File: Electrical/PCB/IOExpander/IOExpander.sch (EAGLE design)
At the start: 38 parts, among them U1 MCP23017T-E/SS

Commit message: PCB Batch #1
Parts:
- added A0A1, A2A3, A4A5, A6A7, IA16, IA17, IA18, IA19, IA20, IA21, IA22, IA23, IB16, IB17, IB18, IB19, IB20, IB21, IB22, IB23: JST_1.25_3P, Scott-Connectors:JST_1.25_3P
- added F1, F3: (no value), Scott-Electrical:FUSE-0603
- added H1, H2, H3, H4: HOLE-M3, Scott-Mechanical:HOLE-M3
- added LA16, LA17, LA18, LA19, LA20, LA21, LA22, LA23, LB16, LB17, LB18, LB19, LB20, LB21, LB22, LB23: JST_1.25_2P, Scott-Connectors:JST_1.25_2P
- added MCU2: JST_1.25_6P, Scott-Connectors:JST_1.25_6P
- added R1, R17, R19, R21, R23, R24, R3, R5, R7, R8: DNP, Scott-Electrical:RESISTOR0603
- added R18, R2, R20, R22, R4, R6: 10K, Scott-Electrical:RESISTOR0603
- added RA5, RA6: (no value), Scott-Electrical:RESISTOR_ARRAY_1206_SEPARATE
- added RB5, RB6: (no value), Scott-Electrical:RESISTOR_ARRAY_1206_SEPARATE_REVERSE
- added U3: MCP23017T-E/SS, Scott-ICs:MCP23017T-E/SS
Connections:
- new net ADDR0: R1.1, R2.2, U1.A0
- new net ADDR0_2: R17.1, R18.2, U3.A0
- new net ADDR1: R3.1, R4.2, U1.A1
- new net ADDR1_2: R19.1, R20.2, U3.A1
- new net ADDR2: R5.1, R6.2, U1.A2
- new net ADDR2_2: R21.1, R22.2, U3.A2
- new net C0: IA23.1, LA23.2, RA5@4.2
- new net C1: IA16.1, LA16.2, RA5@3.2
- new net C2: IA17.1, LA17.2, RA5@2.2
- new net C3: IA18.1, LA18.2, RA5@1.2
- new net C4: IA19.1, LA19.2, RA6@4.2
- new net C5: IA20.1, LA20.2, RA6@3.2
- new net C6: IA21.1, LA21.2, RA6@2.2
- new net C7: IA22.1, LA22.2, RA6@1.2
- new net D0: IB23.1, LB23.2, RB5@4.1
- new net D1: IB16.1, LB16.2, RB5@3.1
- new net D2: IB17.1, LB17.2, RB5@2.1
- new net D3: IB18.1, LB18.2, RB5@1.1
- new net D4: IB19.1, LB19.2, RB6@4.1
- new net D5: IB20.1, LB20.2, RB6@3.1
- new net D6: IB21.1, LB21.2, RB6@2.1
- new net D7: IB22.1, LB22.2, RB6@1.1
- new net INTC: MCU2.2, U3.INTA
- new net INTD: MCU2.1, U3.INTB
- new net N$35: RB5@1.2, U3.GPB3
- new net N$36: RB5@2.2, U3.GPB2
- new net N$37: RB5@3.2, U3.GPB1
- new net N$38: RB5@4.2, U3.GPB0
- new net N$39: RB6@1.2, U3.GPB7
- new net N$40: RB6@2.2, U3.GPB6
- new net N$41: RB6@3.2, U3.GPB5
- new net N$42: RB6@4.2, U3.GPB4
- new net N$43: RA5@1.1, U3.GPA3
- new net N$46: RA5@4.1, U3.GPA0
- new net N$47: RA6@1.1, U3.GPA7
- new net N$48: RA6@2.1, U3.GPA6
- new net N$49: RA6@3.1, U3.GPA5
- new net N$50: RA6@4.1, U3.GPA4
- new net N$51: F3.2, MCU2.6
- new net N$9: F1.2, MCU.6
- net 3.3V: now also F1.1, F3.1, IA16.3, IA17.3, IA18.3, IA19.3, IA20.3, IA21.3, IA22.3, IA23.3, IB0.3, IB1.3, IB16.3, IB17.3, IB18.3, IB19.3, IB2.3, IB20.3, IB21.3, IB22.3, IB23.3, IB3.3, IB4.3, IB5.3, IB6.3, IB7.3, R1.2, R17.2, R19.2, R21.2, R23.1, R24.1, R3.2, R5.2, R7.1, R8.1, U3.!RESET, U3.VDD; no longer MCU.6
- net A0: now also A0A1.3
- net A1: now also A0A1.1
- net A2: now also A2A3.3
- net A3: now also A2A3.1
- net A4: now also A4A5.3
- net A5: now also A4A5.1
- net A6: now also A6A7.3
- net A7: now also A6A7.1
- net GND: now also A0A1.2, A2A3.2, A4A5.2, A6A7.2, IA16.2, IA17.2, IA18.2, IA19.2, IA20.2, IA21.2, IA22.2, IA23.2, IB0.2, IB1.2, IB16.2, IB17.2, IB18.2, IB19.2, IB2.2, IB20.2, IB21.2, IB22.2, IB23.2, IB3.2, IB4.2, IB5.2, IB6.2, IB7.2, LA16.1, LA17.1, LA18.1, LA19.1, LA20.1, LA21.1, LA22.1, LA23.1, LB16.1, LB17.1, LB18.1, LB19.1, LB20.1, LB21.1, LB22.1, LB23.1, MCU2.5, R18.1, R2.1, R20.1, R22.1, R4.1, R6.1, U3.VSS; no longer U1.A0, U1.A1, U1.A2
- net N$44: now also RA5@2.1, U3.GPA2; no longer IB0.3, IB1.3, IB2.3, IB3.3, IB4.3, IB5.3, IB6.3, IB7.3
- net N$45: now also RA5@3.1, U3.GPA1; no longer IB0.2, IB1.2, IB2.2, IB3.2, IB4.2, IB5.2, IB6.2, IB7.2
- net SCL: now also MCU2.3, R23.2, R7.2, U3.SCK
- net SDA: now also MCU2.4, R24.2, R8.2, U3.SDA
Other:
- note added: "A0,A1,A2 Controls address See Page 8 of http://ww1.microchip.com/downloads/en/devicedoc/20001952c.pdf"

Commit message: bump pcb 2/24
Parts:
- removed LB0, LB1, LB2, LB3, LB4, LB5, LB6, LB7: JST_1.25_2P, Scott-Connectors:JST_1.25_2P
- removed MCU: JST_1.25_6P, Scott-Connectors:JST_1.25_6P
- added J0, J1, J2, J3, J4, J5, J6, J7: DNP, Scott-Electrical:RESISTOR0603
- added MCU1: JST_1.25_7P, Scott-Connectors:JST_1.25_7P
- added UD0, UD1, UD2, UD3, UD4, UD5, UD6, UD7: DEBOUNCE_MAX6816EUS+T, Scott-ICs:DEBOUNCE_MAX6816EUS+T
- MCU2: value JST_1.25_6P -> JST_1.25_7P; device Scott-Connectors:JST_1.25_6P -> Scott-Connectors:JST_1.25_7P
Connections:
- removed net N$51: F3.2, MCU2.6
- new net B0D: J3.2, RB1@4.1, UD0.OUT
- new net B1D: J2.2, RB1@3.1, UD1.OUT
- new net B2D: J1.2, RB1@2.1, UD2.OUT
- new net B3D: J0.2, RB1@1.1, UD3.OUT
- new net B4D: J7.2, RB2@4.1, UD4.OUT
- new net B5D: J6.2, RB2@3.1, UD5.OUT
- new net B6D: J5.2, RB2@2.1, UD6.OUT
- new net B7D: J4.2, RB2@1.1, UD7.OUT
- new net N$18: F3.2, MCU2.7
- new net RST1: MCU1.1, U1.!RESET
- new net RST2: MCU2.1, U3.!RESET
- net 3.3V: now also UD0.VCC, UD1.VCC, UD2.VCC, UD3.VCC, UD4.VCC, UD5.VCC, UD6.VCC, UD7.VCC; no longer U1.!RESET, U3.!RESET
- net B0: now also IB3.1, J3.1, UD0.IN; no longer IB0.1, LB0.2, RB1@4.1
- net B1: now also IB2.1, J2.1, UD1.IN; no longer IB1.1, LB1.2, RB1@3.1
- net B2: now also IB1.1, J1.1, UD2.IN; no longer IB2.1, LB2.2, RB1@2.1
- net B3: now also IB0.1, J0.1, UD3.IN; no longer IB3.1, LB3.2, RB1@1.1
- net B4: now also IB7.1, J7.1, UD4.IN; no longer IB4.1, LB4.2, RB2@4.1
- net B5: now also IB6.1, J6.1, UD5.IN; no longer IB5.1, LB5.2, RB2@3.1
- net B6: now also IB5.1, J5.1, UD6.IN; no longer IB6.1, LB6.2, RB2@2.1
- net B7: now also IB4.1, J4.1, UD7.IN; no longer IB7.1, LB7.2, RB2@1.1
- net GND: now also MCU1.6, MCU2.6, UD0.GND, UD1.GND, UD2.GND, UD3.GND, UD4.GND, UD5.GND, UD6.GND, UD7.GND; no longer LB0.1, LB1.1, LB2.1, LB3.1, LB4.1, LB5.1, LB6.1, LB7.1, MCU.5, MCU2.5
- net INTA: now also MCU1.3; no longer MCU.2
- net INTB: now also MCU1.2; no longer MCU.1
- net INTC: now also MCU2.3; no longer MCU2.2
- net INTD: now also MCU2.2; no longer MCU2.1
- net N$9: now also MCU1.7; no longer MCU.6
- net SCL: now also MCU1.4, MCU2.4; no longer MCU.3, MCU2.3
- net SDA: now also MCU1.5, MCU2.5; no longer MCU.4, MCU2.4

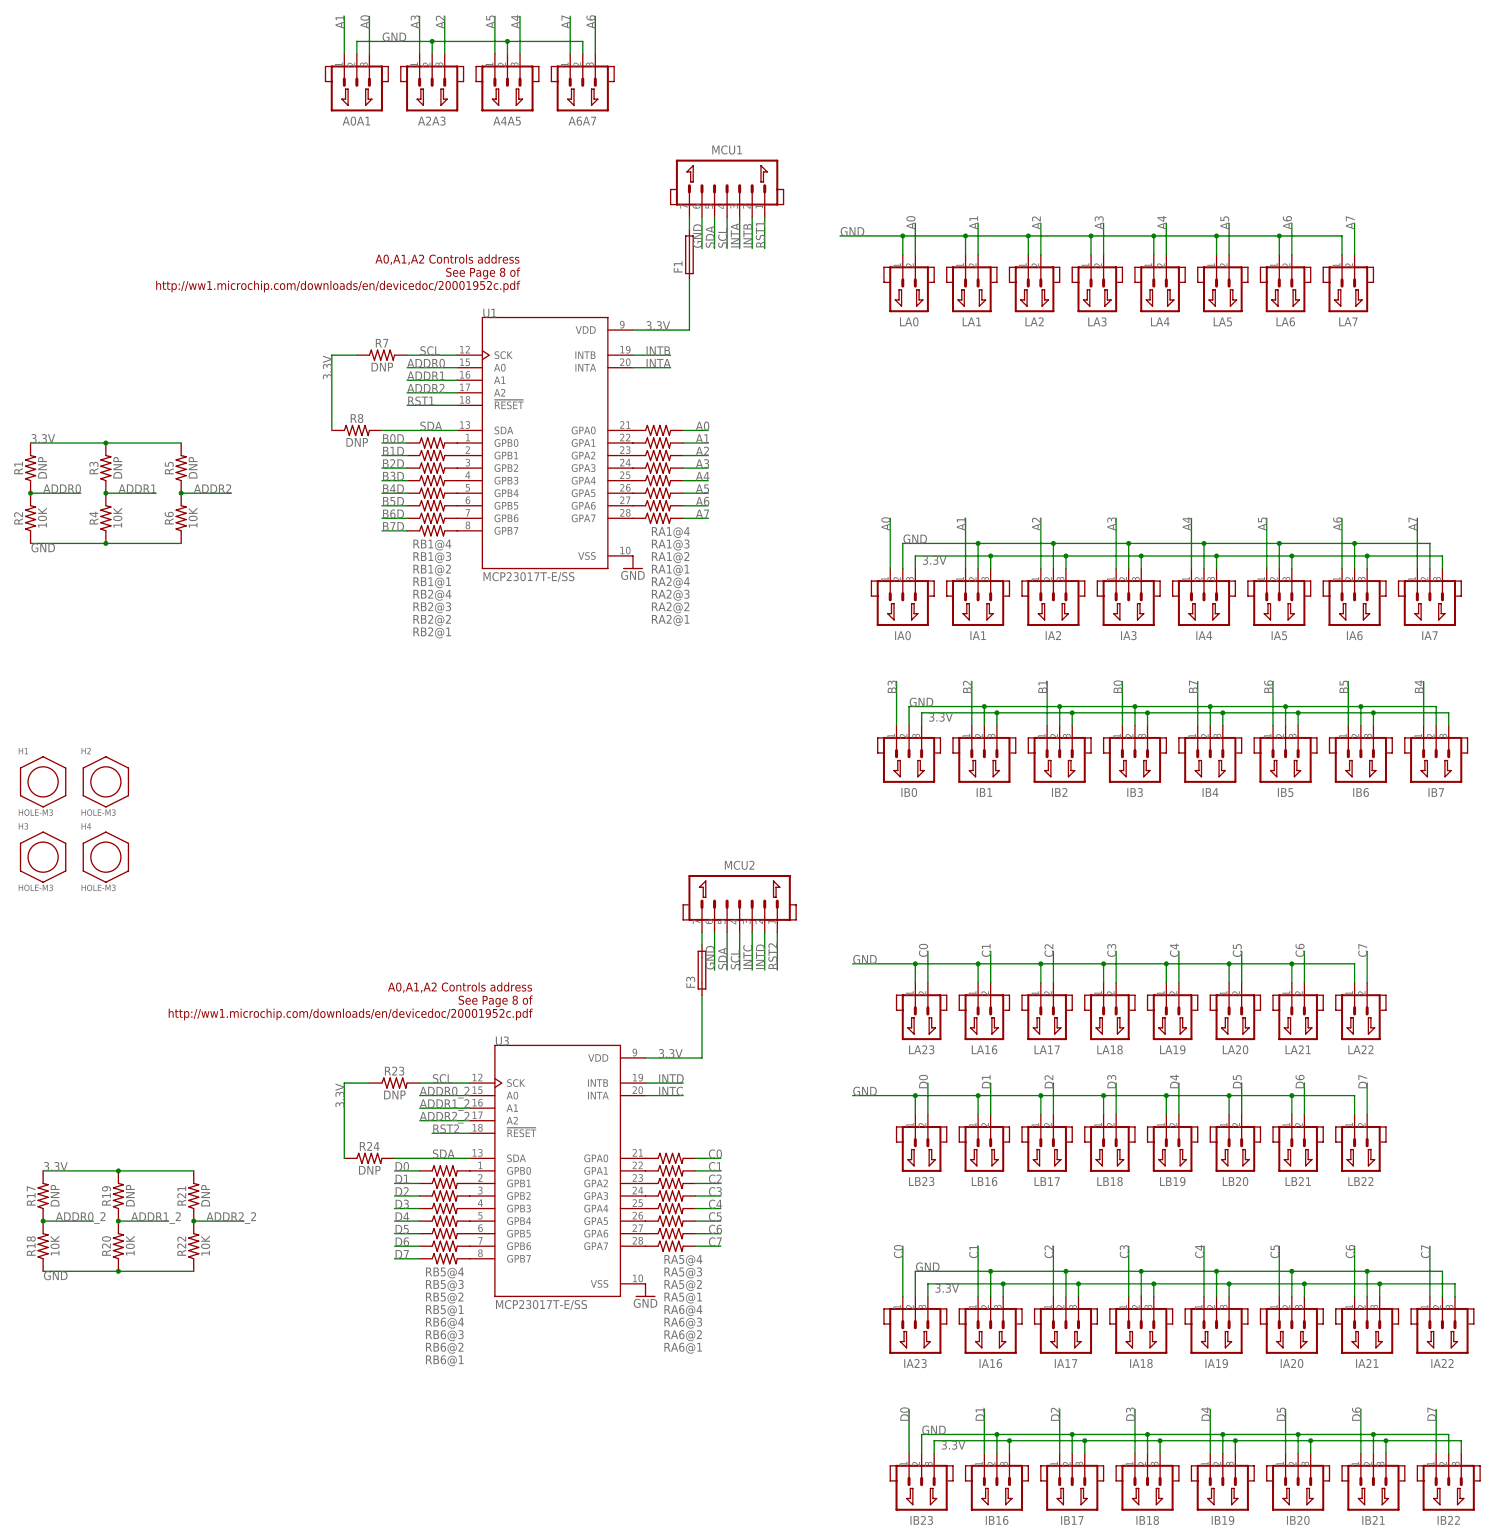
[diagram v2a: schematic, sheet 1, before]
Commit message: io expander fix V2.2 -- add 0.1uF to GND on IRQ pin
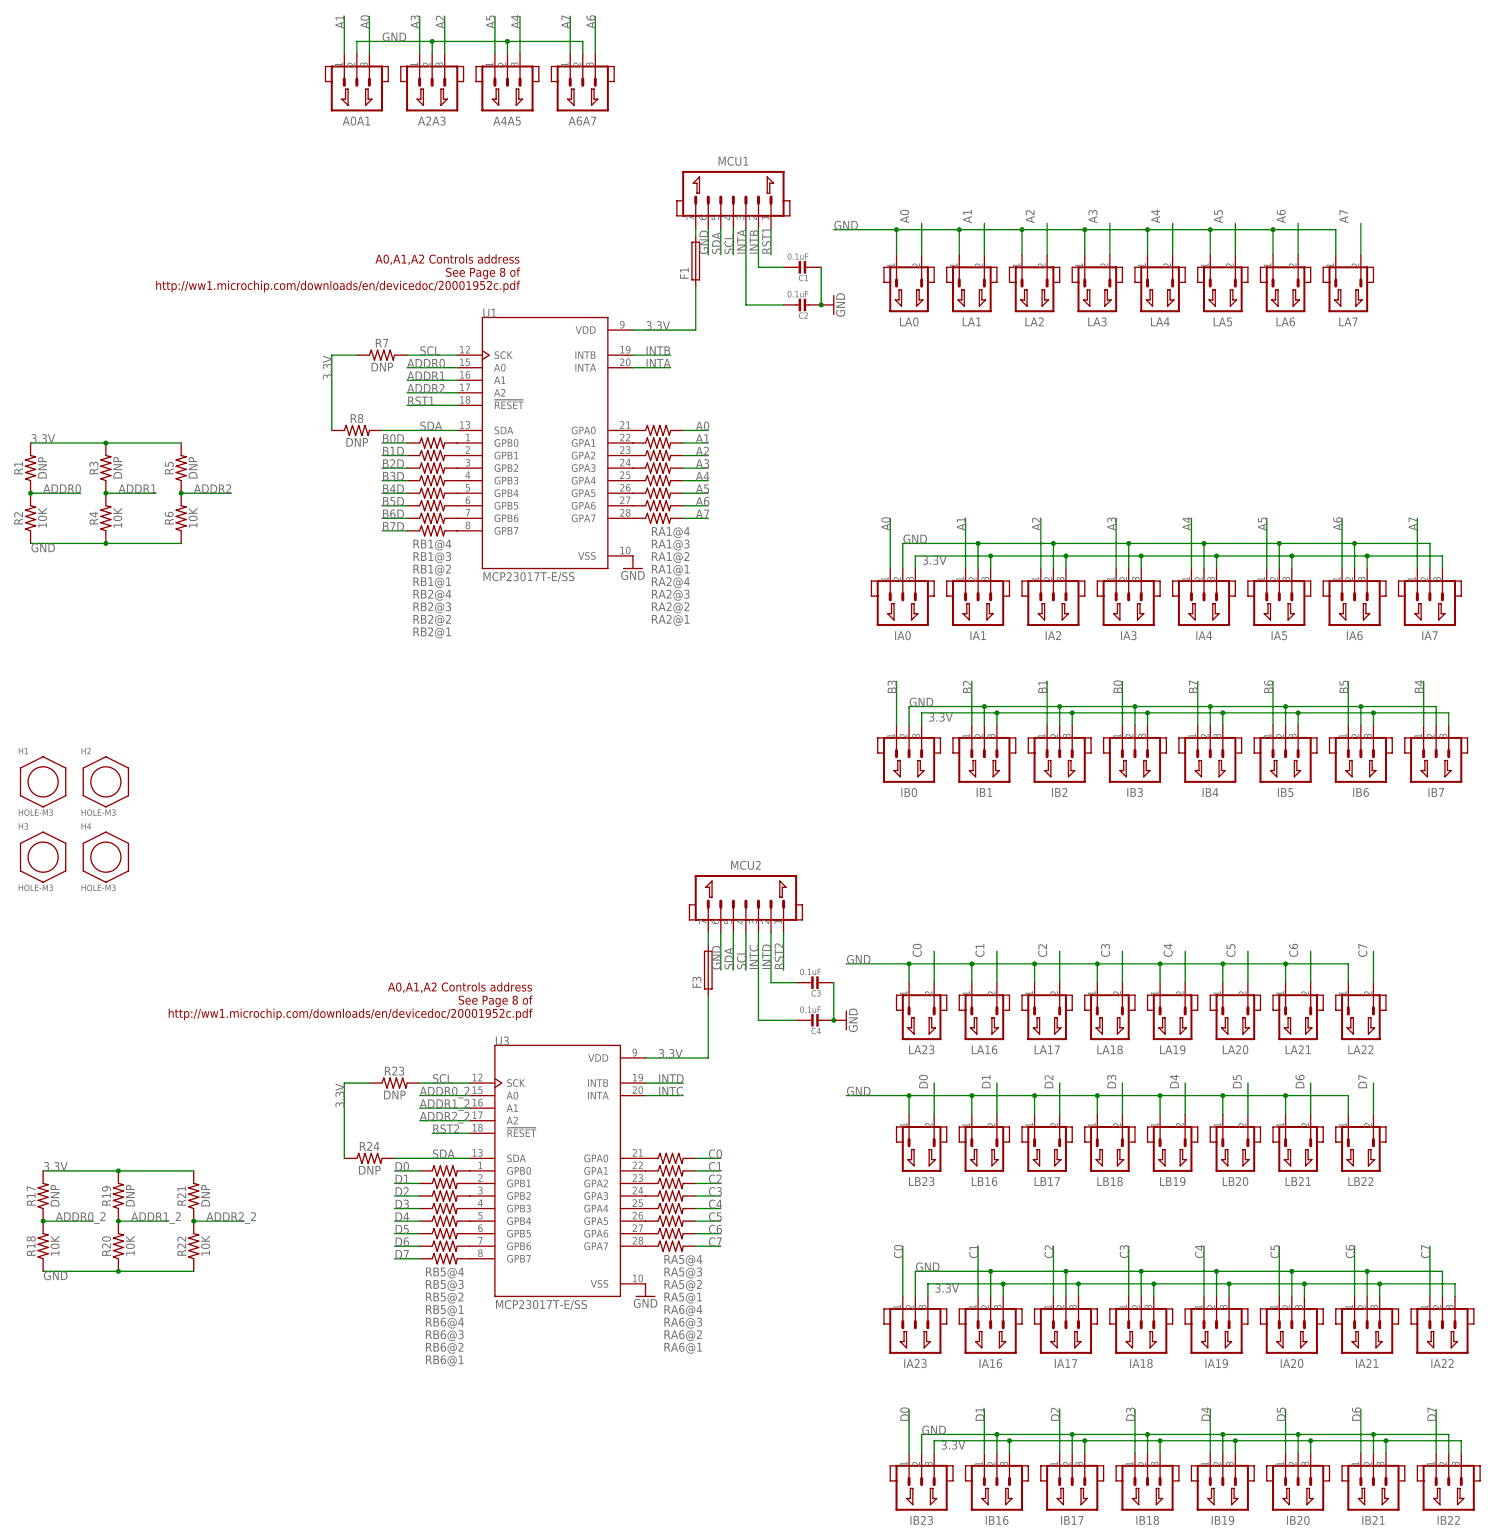
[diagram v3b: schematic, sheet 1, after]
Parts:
- added C1, C2, C3, C4: 0.1uF, Scott-Electrical:CAP_CERAMIC_0603
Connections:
- net GND: now also C1.2, C2.2, C3.2, C4.2
- net INTA: now also C2.1
- net INTB: now also C1.1
- net INTC: now also C4.1
- net INTD: now also C3.1
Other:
- moved on the sheet: F1, F3, MCU1, MCU2
